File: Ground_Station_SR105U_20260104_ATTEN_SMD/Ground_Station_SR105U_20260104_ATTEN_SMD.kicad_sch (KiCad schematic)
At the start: 36 parts, among them J10 SC1464-ND, J11 SC1464-ND, J12 SQ, J2 SQ, J3 Conn_02x03_Odd_Even, J4 Conn_01x03, J5 Conn_01x03, J6 Conn_02x03_Odd_Even, J7 SQ, J8 Conn_01x20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

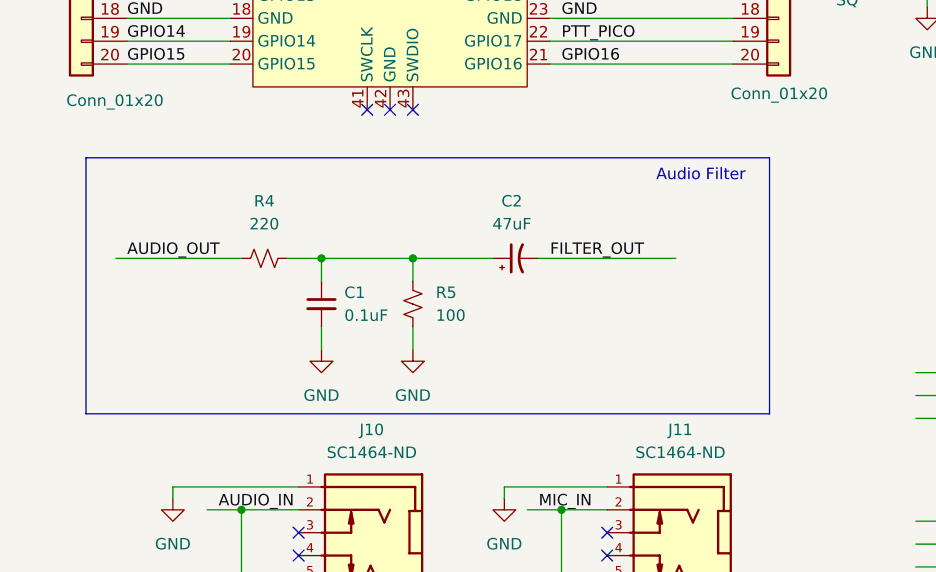
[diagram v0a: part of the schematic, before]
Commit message: Add test points for audio filter
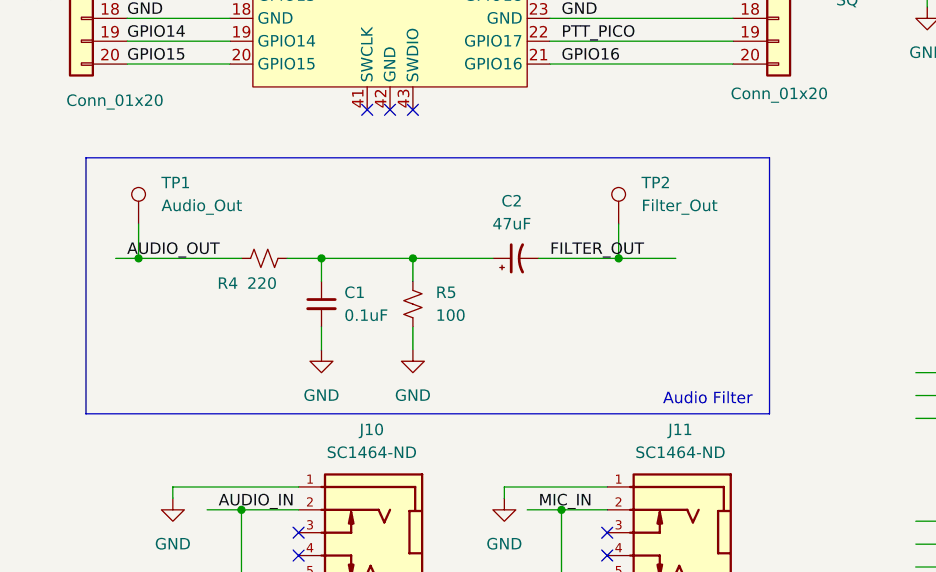
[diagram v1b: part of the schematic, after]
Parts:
- added TP1: Audio_Out, AMSAT:TestPoint_THTPad_D1.5mm_Drill0.7mm, symbol Connector:TestPoint
- added TP2: Filter_Out, AMSAT:TestPoint_THTPad_D1.5mm_Drill0.7mm, symbol Connector:TestPoint
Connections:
- net AUDIO_OUT: now also TP1.1
- net FILTER_OUT: now also TP2.1
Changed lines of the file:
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@@
 	(text "Audio Filter"
 		(exclude_from_sim no)
-		(at 91.694 87.376 0)
+		(at 92.456 112.268 0)
 		(effects
 			(font
@@
 	)
 	(junction
+		(at 29.21 96.52)
+		(diameter 0)
+		(color 0 0 0 0)
+	)
+	(junction
 		(at 76.2 124.46)
 		(diameter 0)
@@
 	)
 	(junction
+		(at 82.55 96.52)
+		(diameter 0)
+		(color 0 0 0 0)
+	)
+	(junction
 		(at 140.97 74.93)
 		(diameter 0)
@@
 	(wire
 		(pts
+			(xy 82.55 96.52) (xy 88.9 96.52)
+		)
+		(stroke
+			(width 0)
+			(type default)
+		)
+	)
+	(wire
+		(pts
 			(xy 149.86 74.93) (xy 173.99 74.93)
 		)
@@
 	(wire
 		(pts
+			(xy 82.55 92.71) (xy 82.55 96.52)
+		)
+		(stroke
+			(width 0)
+			(type default)
+		)
+	)
+	(wire
+		(pts
 			(xy 191.77 140.97) (xy 198.12 140.97)
 		)
@@
 	(wire
 		(pts
+			(xy 29.21 92.71) (xy 29.21 96.52)
+		)
+		(stroke
+			(width 0)
+			(type default)
+		)
+	)
+	(wire
+		(pts
 			(xy 214.63 24.13) (xy 233.68 24.13)
 		)
@@
 	(wire
 		(pts
-			(xy 26.67 96.52) (xy 40.64 96.52)
+			(xy 26.67 96.52) (xy 29.21 96.52)
 		)
 		(stroke
@@
 	(wire
 		(pts
+			(xy 29.21 96.52) (xy 40.64 96.52)
+		)
+		(stroke
+			(width 0)
+			(type default)
+		)
+	)
+	(wire
+		(pts
 			(xy 27.94 72.39) (xy 39.37 72.39)
 		)
@@
 	(wire
 		(pts
-			(xy 73.66 96.52) (xy 88.9 96.52)
+			(xy 73.66 96.52) (xy 82.55 96.52)
 		)
 		(stroke
@@
 	)
 	(symbol
+		(lib_id "Connector:TestPoint")
+		(at 29.21 92.71 0)
+		(unit 1)
+		(exclude_from_sim no)
+		(in_bom yes)
+		(on_board yes)
+		(dnp no)
+		(fields_autoplaced yes)
+		(property "Reference" "TP1"
+			(at 31.75 88.1379 0)
+			(effects
+				(font
+					(size 1.27 1.27)
+				)
+				(justify left)
+			)
+		)
+		(property "Value" "Audio_Out"
+			(at 31.75 90.6779 0)
+			(effects
+				(font
+					(size 1.27 1.27)
+				)
+				(justify left)
+			)
+		)
+		(property "Footprint" "AMSAT:TestPoint_THTPad_D1.5mm_Drill0.7mm"
+			(at 34.29 92.71 0)
+			(effects
+				(font
+					(size 1.27 1.27)
+				)
+				(hide yes)
+			)
+		)
+		(property "Datasheet" "~"
+			(at 34.29 92.71 0)
+			(effects
+				(font
+					(size 1.27 1.27)
+				)
+				(hide yes)
+			)
+		)
+		(property "Description" "test point"
+			(at 29.21 92.71 0)
+			(effects
+				(font
+					(size 1.27 1.27)
+				)
+				(hide yes)
+			)
+		)
+		(pin "1"
+		)
+		(instances
+			(project ""
+				(path "/288fbf00-faaf-4744-be5e-5965d0ade413"
+					(reference "TP1")
+					(unit 1)
+				)
+			)
+		)
+	)
+	(symbol
 		(lib_id "AMSAT:Pico")
 		(at 57.15 50.8 0)
@@
 	)
 	(symbol
+		(lib_id "Connector:TestPoint")
+		(at 82.55 92.71 0)
+		(unit 1)
+		(exclude_from_sim no)
+		(in_bom yes)
+		(on_board yes)
+		(dnp no)
+		(fields_autoplaced yes)
+		(property "Reference" "TP2"
+			(at 85.09 88.1379 0)
+			(effects
+				(font
+					(size 1.27 1.27)
+				)
+				(justify left)
+			)
+		)
+		(property "Value" "Filter_Out"
+			(at 85.09 90.6779 0)
+			(effects
+				(font
+					(size 1.27 1.27)
+				)
+				(justify left)
+			)
+		)
+		(property "Footprint" "AMSAT:TestPoint_THTPad_D1.5mm_Drill0.7mm"
+			(at 87.63 92.71 0)
+			(effects
+				(font
+					(size 1.27 1.27)
+				)
+				(hide yes)
+			)
+		)
+		(property "Datasheet" "~"
+			(at 87.63 92.71 0)
+			(effects
+				(font
+					(size 1.27 1.27)
+				)
+				(hide yes)
+			)
+		)
+		(property "Description" "test point"
+			(at 82.55 92.71 0)
+			(effects
+				(font
+					(size 1.27 1.27)
+				)
+				(hide yes)
+			)
+		)
+		(pin "1"
+		)
+		(instances
+			(project "Ground_Station_SR105U_20260104_ATTEN_SMD"
+				(path "/288fbf00-faaf-4744-be5e-5965d0ade413"
+					(reference "TP2")
+					(unit 1)
+				)
+			)
+		)
+	)
+	(symbol
 		(lib_id "power:GND")
 		(at 59.69 106.68 0)
@@
 		(on_board yes)
 		(dnp no)
-		(fields_autoplaced yes)
 		(property "Reference" "R4"
-			(at 43.18 90.17 90)
+			(at 39.116 99.314 90)
 			(effects
 				(font
@@
 		)
 		(property "Value" "220"
-			(at 43.18 92.71 90)
+			(at 42.926 99.314 90)
 			(effects
 				(font
